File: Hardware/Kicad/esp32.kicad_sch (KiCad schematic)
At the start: 9 parts, among them J5 Micro SD Card Reader, U1 AMS1117-3.3, U4 DEVKIT_V1_ESP32-WROOM-32, U6 ESP32-S3

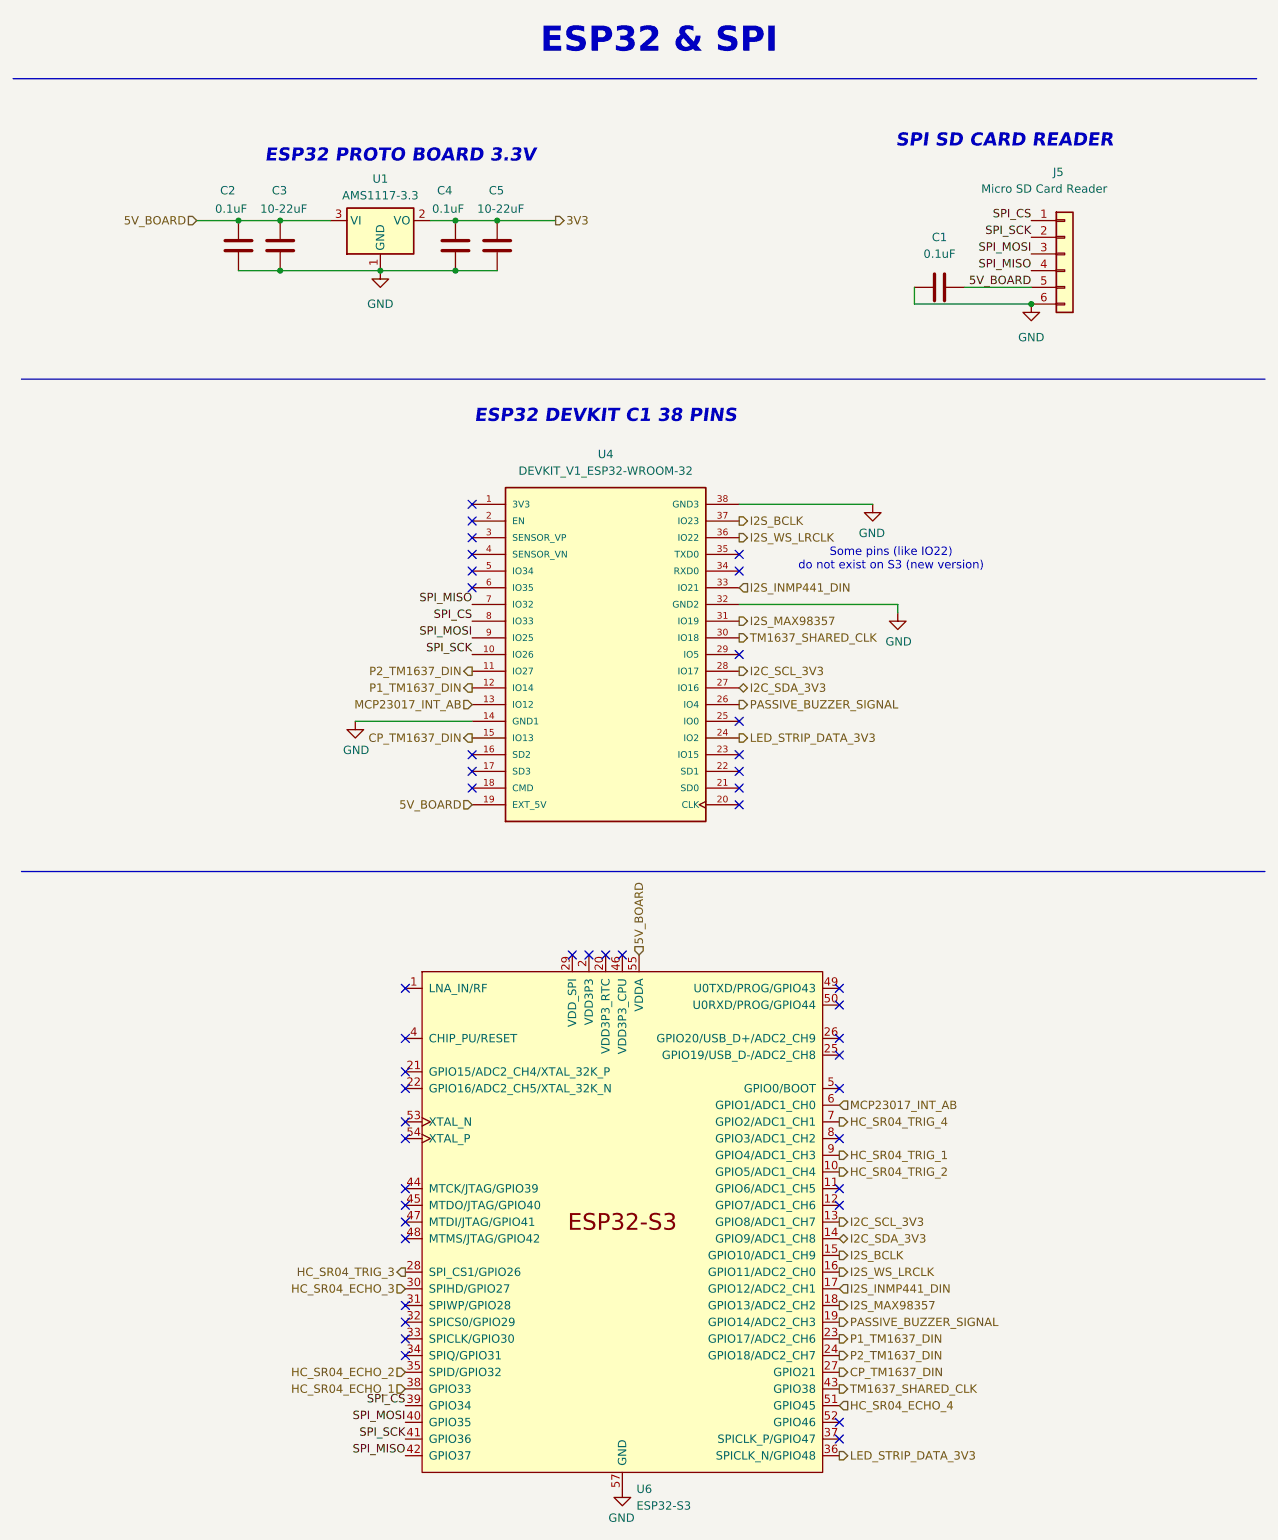
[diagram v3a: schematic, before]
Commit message: Added Kicad proto board
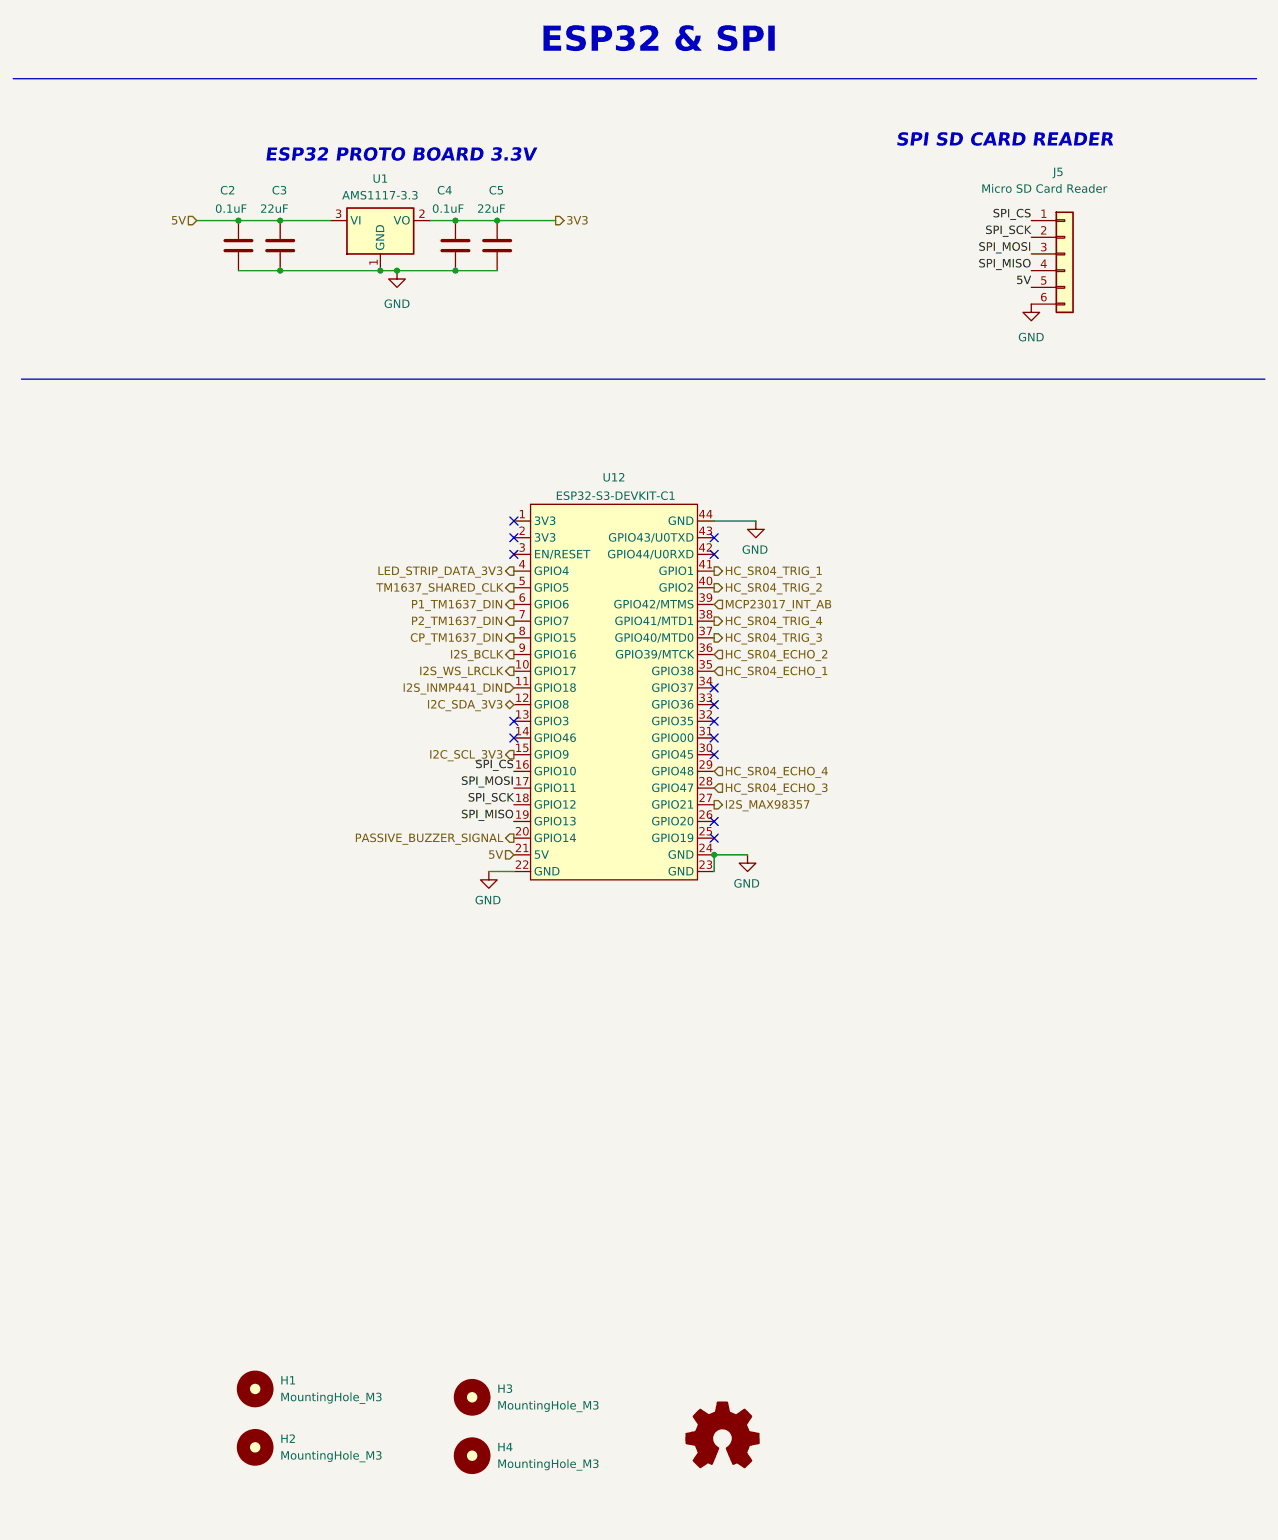
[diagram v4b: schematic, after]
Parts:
- removed C1: 0.1uF, Capacitor_THT:C_Disc_D3.0mm_W1.6mm_P2.50mm, symbol Device:C
- removed U4: DEVKIT_V1_ESP32-WROOM-32, PCM_Espressif:ESP32-DevKitC, symbol DEVKIT_V1_ESP32-WROOM-32:DEVKIT_V1_ESP32-WROOM-32
- removed U6: ESP32-S3, Package_DFN_QFN:QFN-56-1EP_7x7mm_P0.4mm_EP5.6x5.6mm, symbol PCM_Espressif:ESP32-S3
- added H1, H2, H3, H4: MountingHole_M3, MountingHole:MountingHole_3.2mm_M3, symbol PCM_SL_Mechanical:MountingHole_M3
- added U12: ESP32-S3-DEVKIT-C1, PCM_Espressif:ESP32-S3-DevKitC, symbol ESP32_S3_DevKit_New:ESP32-S3-MINI-1-NEW
- C2, C4: footprint Capacitor_THT:C_Disc_D3.0mm_W1.6mm_P2.50mm -> Capacitor_SMD:C_0805_2012Metric_Pad1.18x1.45mm_HandSolder
- C3, C5: value 10-22uF -> 22uF
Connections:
- net CP_TM1637_DIN: now also U12.8 (GPIO15)
- net GND: now also U12.22 (GND), U12.23 (GND), U12.24 (GND), U12.44 (GND)
- net HC_SR04_ECHO_1: now also U12.35 (GPIO38)
- net HC_SR04_ECHO_2: now also U12.36 (GPIO39/MTCK)
- net HC_SR04_ECHO_3: now also U12.28 (GPIO47)
- net HC_SR04_ECHO_4: now also U12.29 (GPIO48)
- net HC_SR04_TRIG_1: now also U12.41 (GPIO1)
- net HC_SR04_TRIG_2: now also U12.40 (GPIO2)
- net HC_SR04_TRIG_3: now also U12.37 (GPIO40/MTD0)
- net HC_SR04_TRIG_4: now also U12.38 (GPIO41/MTD1)
- net I2C_SCL_3V3: now also U12.15 (GPIO9)
- net I2C_SDA_3V3: now also U12.12 (GPIO8)
- net I2S_BCLK: now also U12.9 (GPIO16)
- net I2S_INMP441_DIN: now also U12.11 (GPIO18)
- net I2S_MAX98357: now also U12.27 (GPIO21)
- net I2S_WS_LRCLK: now also U12.10 (GPIO17)
- net LED_STRIP_DATA_3V3: now also U12.4 (GPIO4)
- net MCP23017_INT_AB: now also U12.39 (GPIO42/MTMS)
- net P1_TM1637_DIN: now also U12.6 (GPIO6)
- net P2_TM1637_DIN: now also U12.7 (GPIO7)
- net PASSIVE_BUZZER_SIGNAL: now also U12.20 (GPIO14)
- net SPI_CS: now also U12.16 (GPIO10)
- net SPI_MISO: now also U12.19 (GPIO13)
- net SPI_MOSI: now also U12.17 (GPIO11)
- net SPI_SCK: now also U12.18 (GPIO12)
- net TM1637_SHARED_CLK: now also U12.5 (GPIO5)
- net 5V_BOARD renamed 5V
- net 5V: now also U12.21 (5V)
- no-connect marks 45 -> 14
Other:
- note removed: "ESP32 DEVKIT C1 38 PINS"
- note removed: "Some pins (like IO22) do not exist on S3 (new version)"

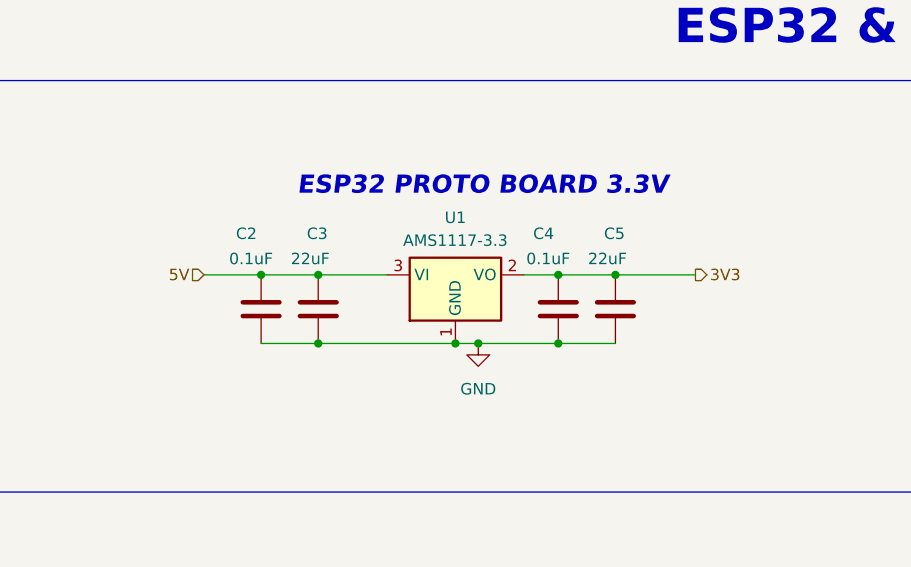
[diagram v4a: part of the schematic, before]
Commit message: New Fraxis PCB layout
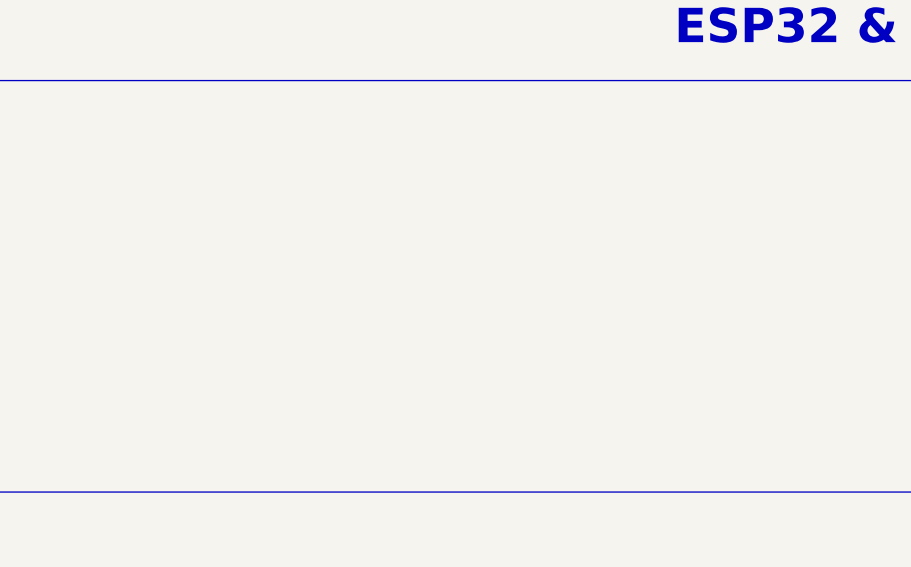
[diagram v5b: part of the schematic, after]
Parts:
- removed C2, C4: 0.1uF, Capacitor_SMD:C_0805_2012Metric_Pad1.18x1.45mm_HandSolder, symbol Device:C
- removed C3, C5: 22uF, Capacitor_THT:CP_Radial_D5.0mm_P2.50mm, symbol Device:C
- removed U1: AMS1117-3.3, Package_TO_SOT_SMD:SOT-223-3_TabPin2, symbol Regulator_Linear:AMS1117-3.3
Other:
- note removed: "ESP32 PROTO BOARD 3.3V"
